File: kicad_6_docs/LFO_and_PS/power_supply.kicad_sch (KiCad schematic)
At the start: 37 parts, among them U1 TL072, U14 LM317_TO-220, U15 LM337_TO220, U3 TL072, U4 TL072, U6 TL072, U7 TL072

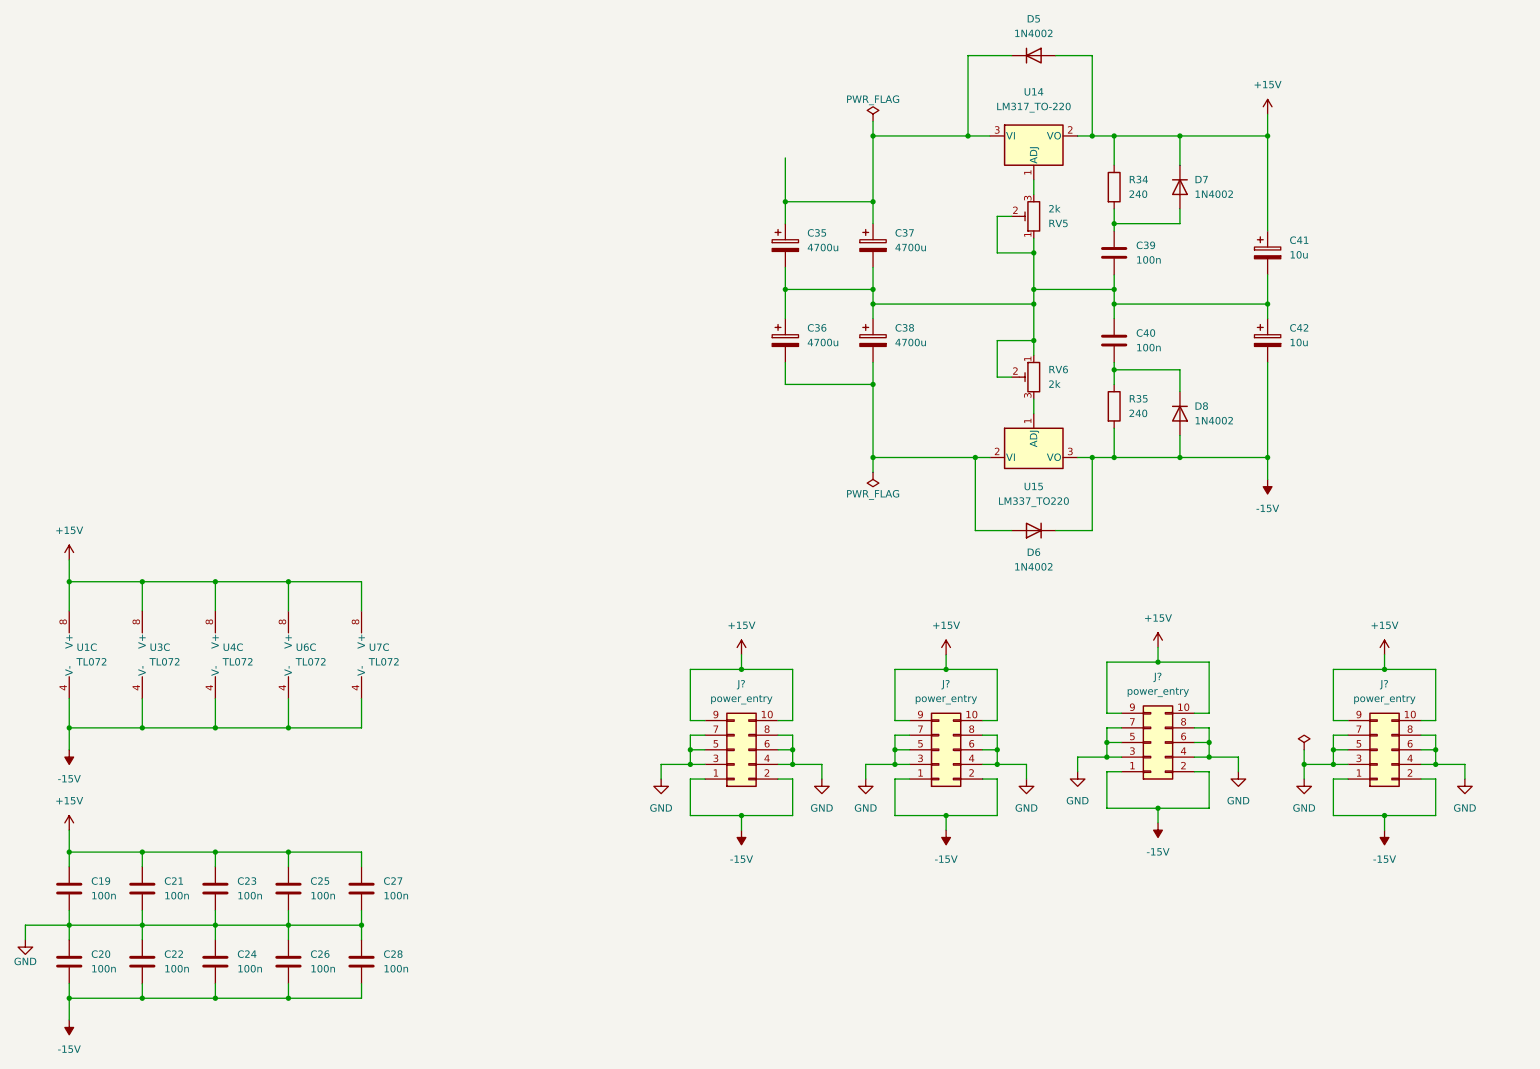
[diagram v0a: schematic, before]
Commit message: Progress on LFO/PS board
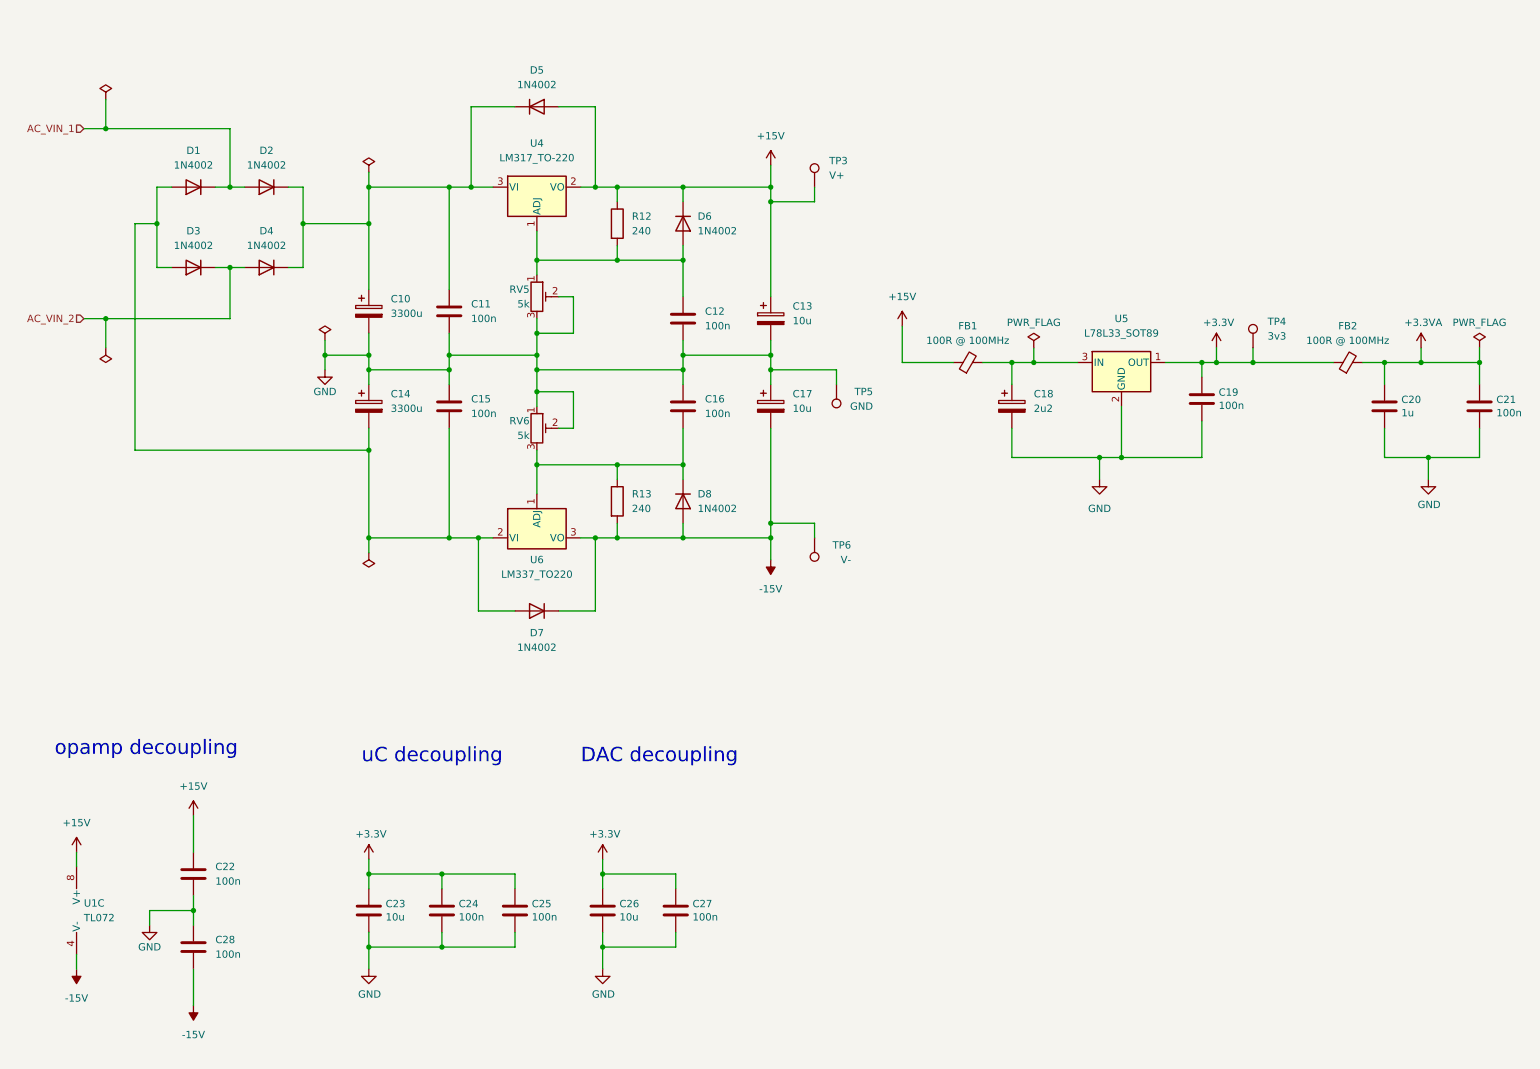
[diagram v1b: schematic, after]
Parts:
- removed C22, C28, C39, C40: 100n, symbol Device:C
- removed C35, C36, C37, C38: 4700u, symbol Device:C_Polarized
- removed C41, C42: 10u, symbol Device:C_Polarized
- removed J? (x4): power_entry, Connector_IDC:IDC-Header_2x05_P2.54mm_Vertical, symbol Connector_Generic:Conn_02x05_Odd_Even
- removed R34, R35: 240, symbol Device:R
- removed U14: LM317_TO-220, Package_TO_SOT_THT:TO-220-3_Vertical, symbol Regulator_Linear:LM317_TO-220
- removed U15: LM337_TO220, Package_TO_SOT_THT:TO-220-3_Vertical, symbol Regulator_Linear:LM337_TO220
- removed U3, U4, U6, U7: TL072, symbol Amplifier_Operational:TL072
- added C10, C14: 3300u, Capacitor_THT:CP_Radial_D17.0mm_P7.50mm, symbol Device:C_Polarized
- added C11, C12, C15, C16, C19: 100n, Capacitor_SMD:C_0805_2012Metric, symbol Device:C
- added C13, C17: 10u, Capacitor_THT:CP_Radial_D6.3mm_P2.50mm, symbol Device:C_Polarized
- added C18: 2u2, Capacitor_THT:CP_Radial_D6.3mm_P2.50mm, symbol Device:C_Polarized
- added C20: 1u, Capacitor_SMD:C_0805_2012Metric, symbol Device:C
- added D1, D2, D3, D4: 1N4002, Diode_THT:D_DO-41_SOD81_P10.16mm_Horizontal, symbol Diode:1N4002
- added FB1, FB2: 100R @ 100MHz, Inductor_SMD:L_0805_2012Metric, symbol Device:FerriteBead_Small
- added R12, R13: 240, Resistor_SMD:R_0805_2012Metric, symbol Device:R
- added TP3: V+, TestPoint:TestPoint_Keystone_5000-5004_Miniature, symbol Connector:TestPoint
- added TP4: 3v3, TestPoint:TestPoint_Keystone_5000-5004_Miniature, symbol Connector:TestPoint
- added TP5: GND, TestPoint:TestPoint_Bridge_Pitch7.62mm_Drill1.3mm, symbol Connector:TestPoint
- added TP6: V-, TestPoint:TestPoint_Keystone_5000-5004_Miniature, symbol Connector:TestPoint
- added U4: LM317_TO-220, Package_TO_SOT_THT:TO-220F-3_Horizontal_TabDown, symbol Regulator_Linear:LM317_TO-220
- added U5: L78L33_SOT89, Package_TO_SOT_SMD:SOT-89-3, symbol Regulator_Linear:L78L33_SOT89
- added U6: LM337_TO220, Package_TO_SOT_THT:TO-220F-3_Horizontal_TabDown, symbol Regulator_Linear:LM337_TO220
- C21, C24, C25, C27: footprint (none) -> Capacitor_SMD:C_0805_2012Metric
- C22: renamed from C19; footprint (none) -> Capacitor_SMD:C_0805_2012Metric
- C23, C26: value 100n -> 10u; footprint (none) -> Capacitor_SMD:C_0805_2012Metric
- C28: renamed from C20; footprint (none) -> Capacitor_SMD:C_0805_2012Metric
- RV5, RV6: value 2k -> 5k; footprint (none) -> Potentiometer_THT:Potentiometer_Bourns_3296W_Vertical
- U1: footprint (none) -> Package_SO:SOIC-8_3.9x4.9mm_P1.27mm
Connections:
- net +15V: now also D6.1 (K), C13.1, FB1.1, R12.1, TP3.1, U4.2 (VO); no longer C21.1, C23.1, C25.1, C27.1, D7.1 (K)
- net -15V: now also D7.1 (K), C17.2, R13.2, TP6.1, U6.3 (VO); no longer C24.2, C26.2, D6.1 (K)
- net GND: now also C24.2, C26.2, RV5.2, RV5.3, RV6.1, RV6.2, C10.2, C11.2, C12.2, C13.2, C14.1, C15.1, C16.1, C17.1, C18.2, C19.2, C20.2, TP5.1, U5.2 (GND); no longer C24.1, C26.1
- net at D6.2 (A): now also RV5.1, C12.1, R12.2, U4.1 (ADJ)
- net at D5.1 (K): now also C10.1, C11.1, D2.1 (K), D4.1 (K), U4.3 (VI)
- net at D7.2 (A): now also C14.2, C15.2, D1.2 (A), D3.2 (A), U6.2 (VI)
- net at D8.1 (K): now also RV6.3, C16.2, R13.1, U6.1 (ADJ)
- new net: C18.1, FB1.2, U5.3 (IN)
- new net +3.3VA: C20.1, C21.1, FB2.2
- new net +3V3: C19.1, C23.1, C24.1, C25.1, C26.1, C27.1, FB2.1, TP4.1, U5.1 (OUT)
- new net AC_VIN_1: D1.1 (K), D2.2 (A)
- new net AC_VIN_2: D3.1 (K), D4.2 (A)
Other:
- note added: "DAC decoupling"
- note added: "opamp decoupling"
- note added: "uC decoupling"
- moved on the sheet: C22, C28, U1C
